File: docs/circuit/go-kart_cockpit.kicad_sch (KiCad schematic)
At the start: 40 parts, among them P1 Power, Q1 IRLIZ44N, SW1 SW_MEC_5E, X1 Taster rechts (male), X10 Display (male), X11 PD7, X12 SDA PG4, X13 AVR-ISP-10, X14 Taster links (male), X15 Start/Stop/Rückwärts, X2 5V GND, X3 24V Hupe, X4 SCL, X5 CS, X6 PB6, X7 J5, X8 J3, X9 Bluetooth-Modul

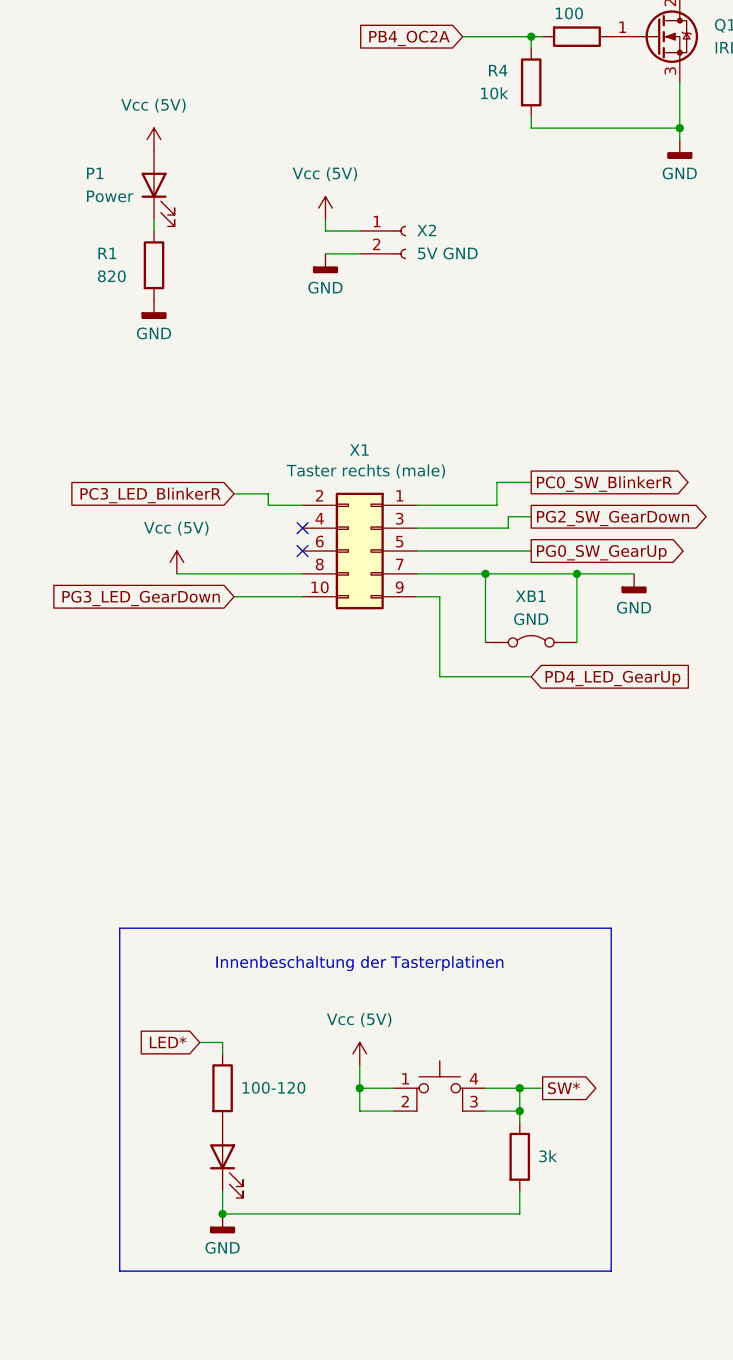
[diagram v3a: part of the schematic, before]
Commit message: feat: cleanup Tasterinnenbeschaltung for presentation
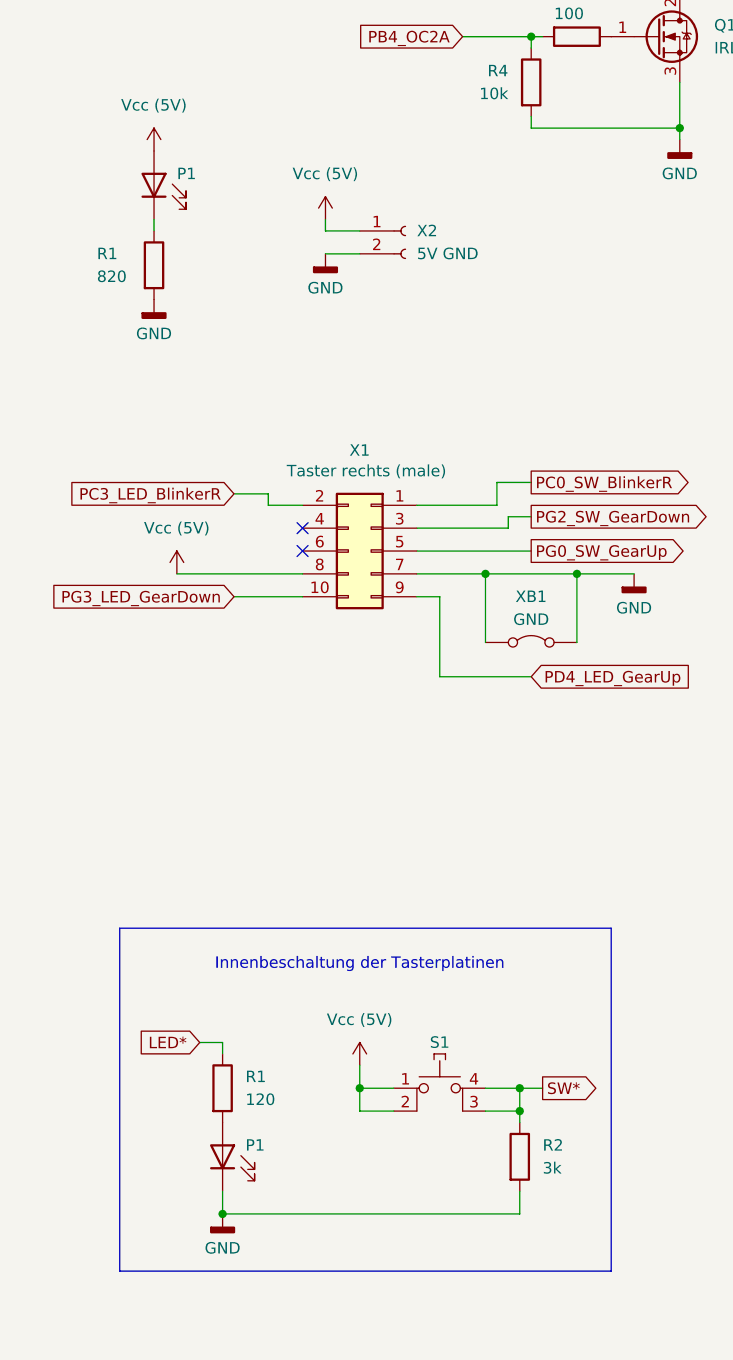
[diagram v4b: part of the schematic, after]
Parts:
- P1: renamed from D1; now left out of the parts list
- P1: value Power -> LED; footprint LED_THT:LED_D3.0mm_Horizontal_O1.27mm_Z6.0mm -> (none)
- R1: renamed from R2; value 100-120 -> 120; now left out of the parts list
- renumbered R3 to R2, SW1 to S1
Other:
- moved on the sheet: P1
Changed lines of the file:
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@@
 	)
 	(symbol
+		(lib_name "LED_1")
 		(lib_id "Device:LED")
 		(at 34.29 175.26 90)
 		(unit 1)
-		(exclude_from_sim no)
-		(in_bom yes)
+		(exclude_from_sim yes)
+		(in_bom no)
 		(on_board no)
 		(dnp no)
-		(fields_autoplaced yes)
-		(property "Reference" "D1"
-			(at 38.1 175.5774 90)
+		(property "Reference" "P1"
+			(at 36.83 173.99 90)
 			(effects
 				(font
@@
 				)
 				(justify right)
-				(hide yes)
 			)
 		)
@@
 			(project ""
 				(path "/e785e5e4-6da9-4e03-ba54-b62675208098"
-					(reference "D1")
+					(reference "P1")
 					(unit 1)
 				)
@@
 		(on_board no)
 		(dnp no)
-		(property "Reference" "R3"
-			(at 69.85 173.9899 0)
+		(property "Reference" "R2"
+			(at 69.85 173.99 0)
 			(effects
 				(font
@@
 				)
 				(justify left)
-				(hide yes)
 			)
 		)
 		(property "Value" "3k"
-			(at 69.342 175.26 0)
+			(at 69.85 176.53 0)
 			(effects
 				(font
@@
 			(project "go-kart_cockpit"
 				(path "/e785e5e4-6da9-4e03-ba54-b62675208098"
-					(reference "R3")
+					(reference "R2")
 					(unit 1)
 				)
@@
 		(dnp no)
 		(property "Reference" "P1"
-			(at 19.05 66.04 90)
+			(at 29.21 66.04 90)
 			(effects
 				(font
@@
 			)
 		)
-		(property "Value" "Power"
-			(at 19.05 68.58 90)
+		(property "Value" "LED"
+			(at 30.48 70.1674 90)
 			(effects
 				(font
@@
 				)
 				(justify right)
+				(hide yes)
 			)
 		)
-		(property "Footprint" "LED_THT:LED_D3.0mm_Horizontal_O1.27mm_Z6.0mm"
+		(property "Footprint" ""
 			(at 26.67 67.31 0)
 			(effects
@@
 		(on_board no)
 		(dnp no)
-		(fields_autoplaced yes)
-		(property "Reference" "SW1"
-			(at 58.42 160.02 0)
+		(property "Reference" "S1"
+			(at 58.42 162.56 0)
 			(effects
 				(font
 					(size 1.27 1.27)
 				)
-				(hide yes)
 			)
 		)
@@
 			(project ""
 				(path "/e785e5e4-6da9-4e03-ba54-b62675208098"
-					(reference "SW1")
+					(reference "S1")
 					(unit 1)
 				)
@@
 		(at 34.29 167.64 0)
 		(unit 1)
-		(exclude_from_sim no)
-		(in_bom yes)
+		(exclude_from_sim yes)
+		(in_bom no)
 		(on_board no)
 		(dnp no)
-		(property "Reference" "R2"
-			(at 36.83 166.3699 0)
+		(property "Reference" "R1"
+			(at 36.83 166.37 0)
 			(effects
 				(font
@@
 				)
 				(justify left)
-				(hide yes)
 			)
 		)
-		(property "Value" "100-120"
-			(at 36.322 167.64 0)
+		(property "Value" "120"
+			(at 36.83 168.91 0)
 			(effects
 				(font
@@
 			(project ""
 				(path "/e785e5e4-6da9-4e03-ba54-b62675208098"
-					(reference "R2")
+					(reference "R1")
 					(unit 1)
 				)

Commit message: feat: rework of PCB, fix wrong connection
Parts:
- removed P1: LED, symbol Device:LED
- removed X11: PD7, Connector_PinSocket_2.54mm:PinSocket_1x01_P2.54mm_Vertical, symbol Connector:Conn_01x01_Socket
- removed X12: SDA PG4, Connector_PinSocket_2.54mm:PinSocket_1x02_P2.54mm_Vertical, symbol Connector:Conn_01x02_Socket
- removed X2: 5V GND, Connector_PinSocket_2.54mm:PinSocket_1x02_P2.54mm_Vertical, symbol Connector:Conn_01x02_Socket
- removed XB10: ISP_SCK, Resistor_THT:R_Axial_DIN0207_L6.3mm_D2.5mm_P10.16mm_Horizontal, symbol Jumper:Jumper_2_Bridged
- removed XB4: Display_GND, Resistor_THT:R_Axial_DIN0207_L6.3mm_D2.5mm_P10.16mm_Horizontal, symbol Jumper:Jumper_2_Bridged
- removed XB5: Display_Vcc, Resistor_THT:R_Axial_DIN0207_L6.3mm_D2.5mm_P15.24mm_Horizontal, symbol Jumper:Jumper_2_Bridged
- removed XB9: ISP_MOSI, Resistor_THT:R_Axial_DIN0207_L6.3mm_D2.5mm_P15.24mm_Horizontal, symbol Jumper:Jumper_2_Bridged
- added P2: Power, LED_THT:LED_D3.0mm_Horizontal_O1.27mm_Z6.0mm, symbol Device:LED
- added X4: PC2 PG1 PD7, Connector_PinSocket_2.54mm:PinSocket_1x03_P2.54mm_Vertical, symbol Connector:Conn_01x03_Socket
- added X7: PD1 PG4 VCC GND, Connector_PinSocket_2.54mm:PinSocket_1x04_P2.54mm_Vertical, symbol Connector:Conn_01x04_Socket
- added XB1, XB6: GND, Resistor_THT:R_Axial_DIN0207_L6.3mm_D2.5mm_P10.16mm_Horizontal, symbol Jumper:Jumper_2_Bridged
- added XB11: MISO, TestPoint:TestPoint_2Pads_Pitch5.08mm_Drill1.3mm, symbol Jumper:Jumper_2_Bridged
- added XB12: /RESET, Resistor_THT:R_Axial_DIN0207_L6.3mm_D2.5mm_P15.24mm_Horizontal, symbol Jumper:Jumper_2_Bridged
- added XB2, XB3: Vcc, Resistor_THT:R_Axial_DIN0207_L6.3mm_D2.5mm_P10.16mm_Horizontal, symbol Jumper:Jumper_2_Bridged
- P1: value LED -> Power; footprint (none) -> LED_THT:LED_D3.0mm_Horizontal_O1.27mm_Z6.0mm
- Q1: value IRLIZ44N -> IRL3803; footprint Library:TO-220-3_Horizontal_TabDown_no_hole -> Package_TO_SOT_THT:TO-220F-3_Horizontal_TabDown
- R3: renamed from R1; footprint Resistor_THT:R_Axial_DIN0207_L6.3mm_D2.5mm_P10.16mm_Horizontal -> Resistor_THT:R_Axial_DIN0309_L9.0mm_D3.2mm_P12.70mm_Horizontal
- R4: renamed from R7; footprint Resistor_THT:R_Axial_DIN0207_L6.3mm_D2.5mm_P15.24mm_Horizontal -> Resistor_THT:R_Axial_DIN0207_L6.3mm_D2.5mm_P10.16mm_Horizontal
- R8: renamed from R1; value 120 -> 100-120; now in the parts list
- R9: renamed from R6; footprint Resistor_THT:R_Axial_DIN0309_L9.0mm_D3.2mm_P25.40mm_Horizontal -> Resistor_THT:R_Axial_DIN0207_L6.3mm_D2.5mm_P7.62mm_Horizontal
- XB4: renamed from XB3; value Display_Vcc -> Vcc
- renumbered R10 to R1, R2 to R10, R4 to R11, R11 to R2, R8 to R5, R9 to R6, R5 to R7, X15 to X1, X5 to X10, X8 to X11, X6 to X12, X3 to X14, X1 to X2, X14 to X3, X4 to X5, X7 to X6, X9 to X8, X10 to X9, XB6 to XB10, XB8 to XB5, XB1 to XB7, XB2 to XB8, XB7 to XB9
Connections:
- net +24V: now also X14.2 (Pin_2); no longer X14.3 (Pin_3)
- net GND: now also P2.1 (K), X7.4 (Pin_4), XB1.1 (A), XB1.2 (B), XB6.1 (A), XB6.2 (B)
- net Hupe (-): now also X14.3 (Pin_3); no longer X14.2 (Pin_2)
- net PB3_MISO: now also XB11.1 (A), XB11.2 (B)
- net PD1_SDA: now also X7.1 (Pin_1)
- net PD7: now also X4.3 (Pin_3)
- net PE0_RXD0: now also X9.2 (Pin_2); no longer X9.6 (Pin_6)
- net PE1_TXD0: now also X9.6 (Pin_6); no longer X9.2 (Pin_2)
- net PG4: now also X7.2 (Pin_2)
- net Vcc (5V): now also X7.3 (Pin_3), XB2.1 (A), XB2.2 (B), XB3.1 (A), XB3.2 (B)
- net /RESET: now also XB12.1 (A), XB12.2 (B)
- net at R8.2: now also P2.2 (A)
- net /PB7_SW_Reverse: now reaches X11.11 (Pin_11)
- net /PB7_SW_Reverse: now also R1.1
- net /PB5_SW_Start: now reaches X11.13 (Pin_13)
- net /PB5_SW_Start: now also R2.1
- net /PC2_SW_Start renamed PC2
- net PC2: now also X4.1 (Pin_1); no longer R2.1
- net /PG1_SW_Reverse renamed PG1
- net PG1: now also X4.2 (Pin_2); no longer R1.1
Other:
- moved on the sheet: P1, Q1, R1, R10, R11, R2, R3, R4, R5, R6, R7, R8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

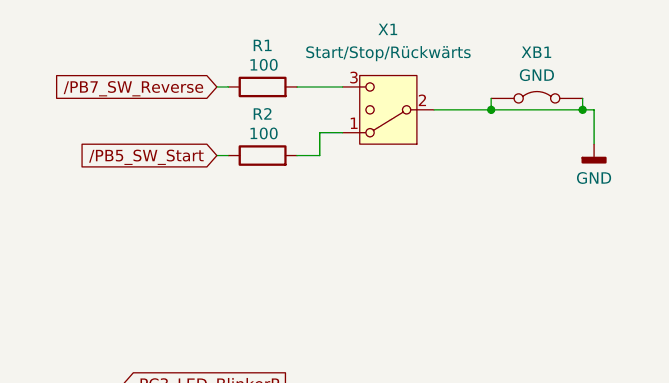
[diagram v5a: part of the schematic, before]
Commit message: feat(PCB): replace 100 ohm preresistors with 330
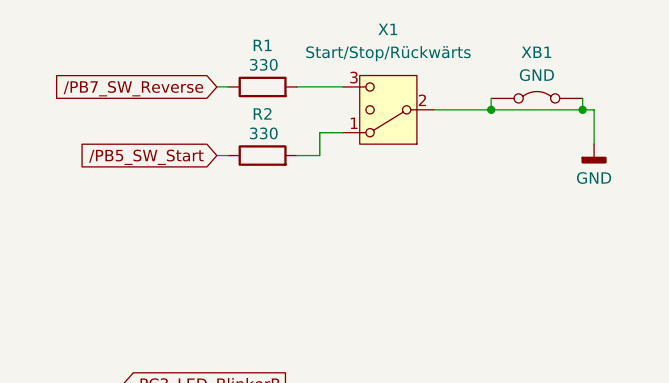
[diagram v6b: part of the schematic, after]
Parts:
- R1, R2: value 100 -> 330
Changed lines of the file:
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@@
 			)
 		)
-		(property "Value" "100"
+		(property "Value" "330"
 			(at 42.037 34.417 90)
 			(effects
@@
 			)
 		)
-		(property "Value" "100"
+		(property "Value" "330"
 			(at 42.037 26.797 90)
 			(effects

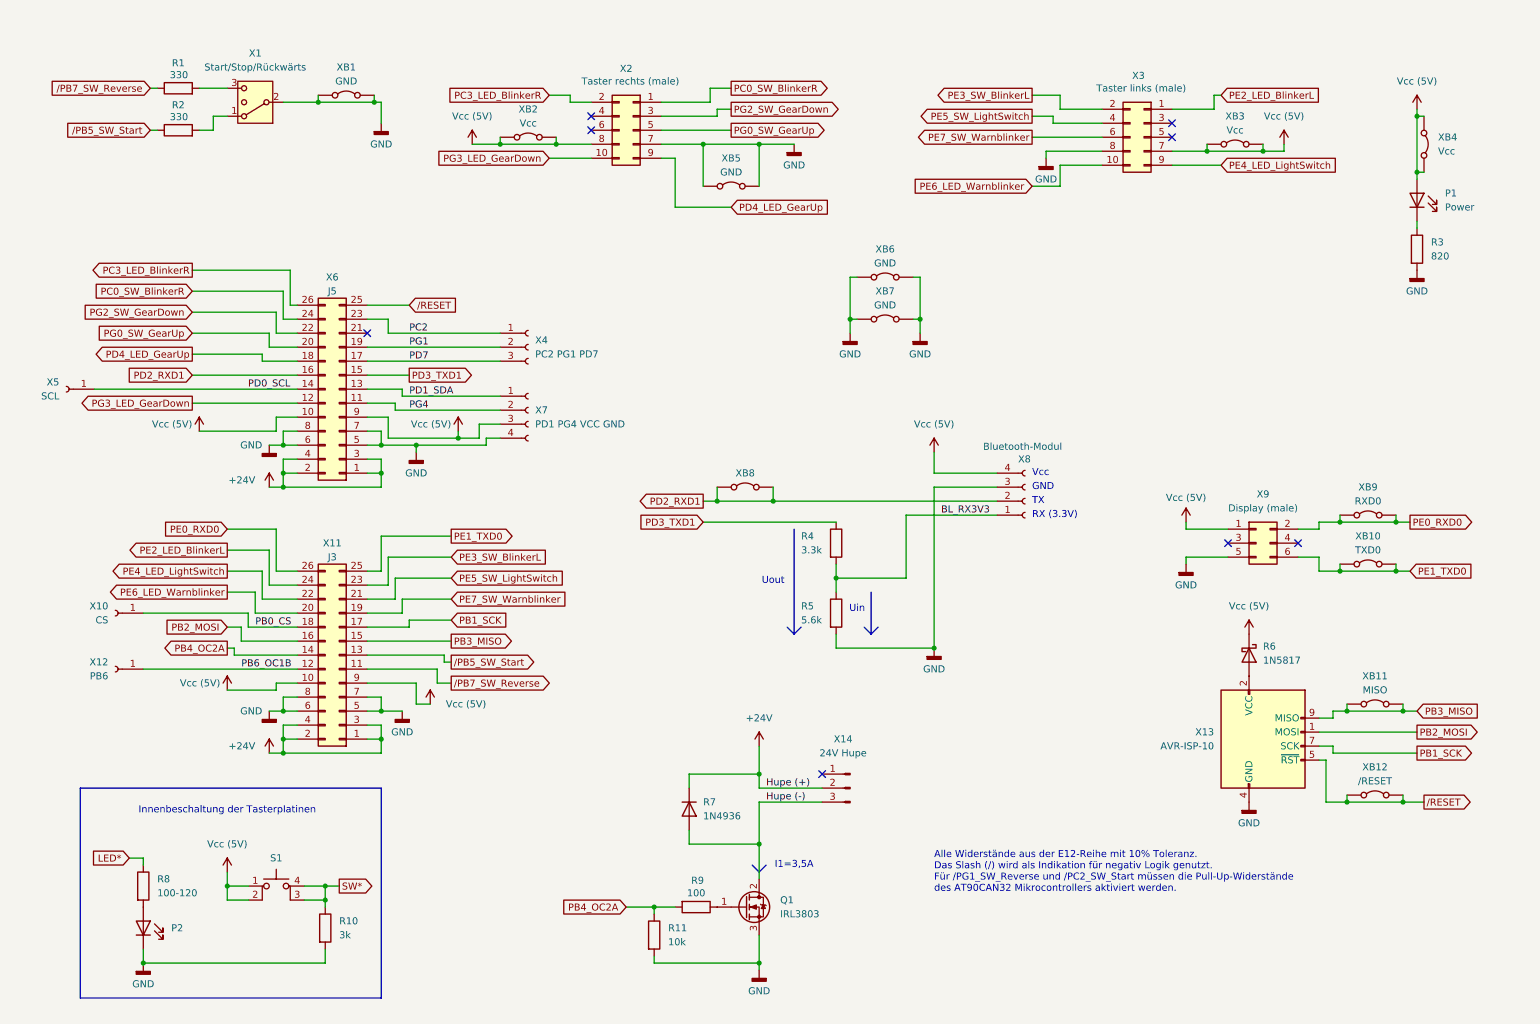
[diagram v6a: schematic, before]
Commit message: fix(PCB): ISP is actually connected to UART0 instead of SPI
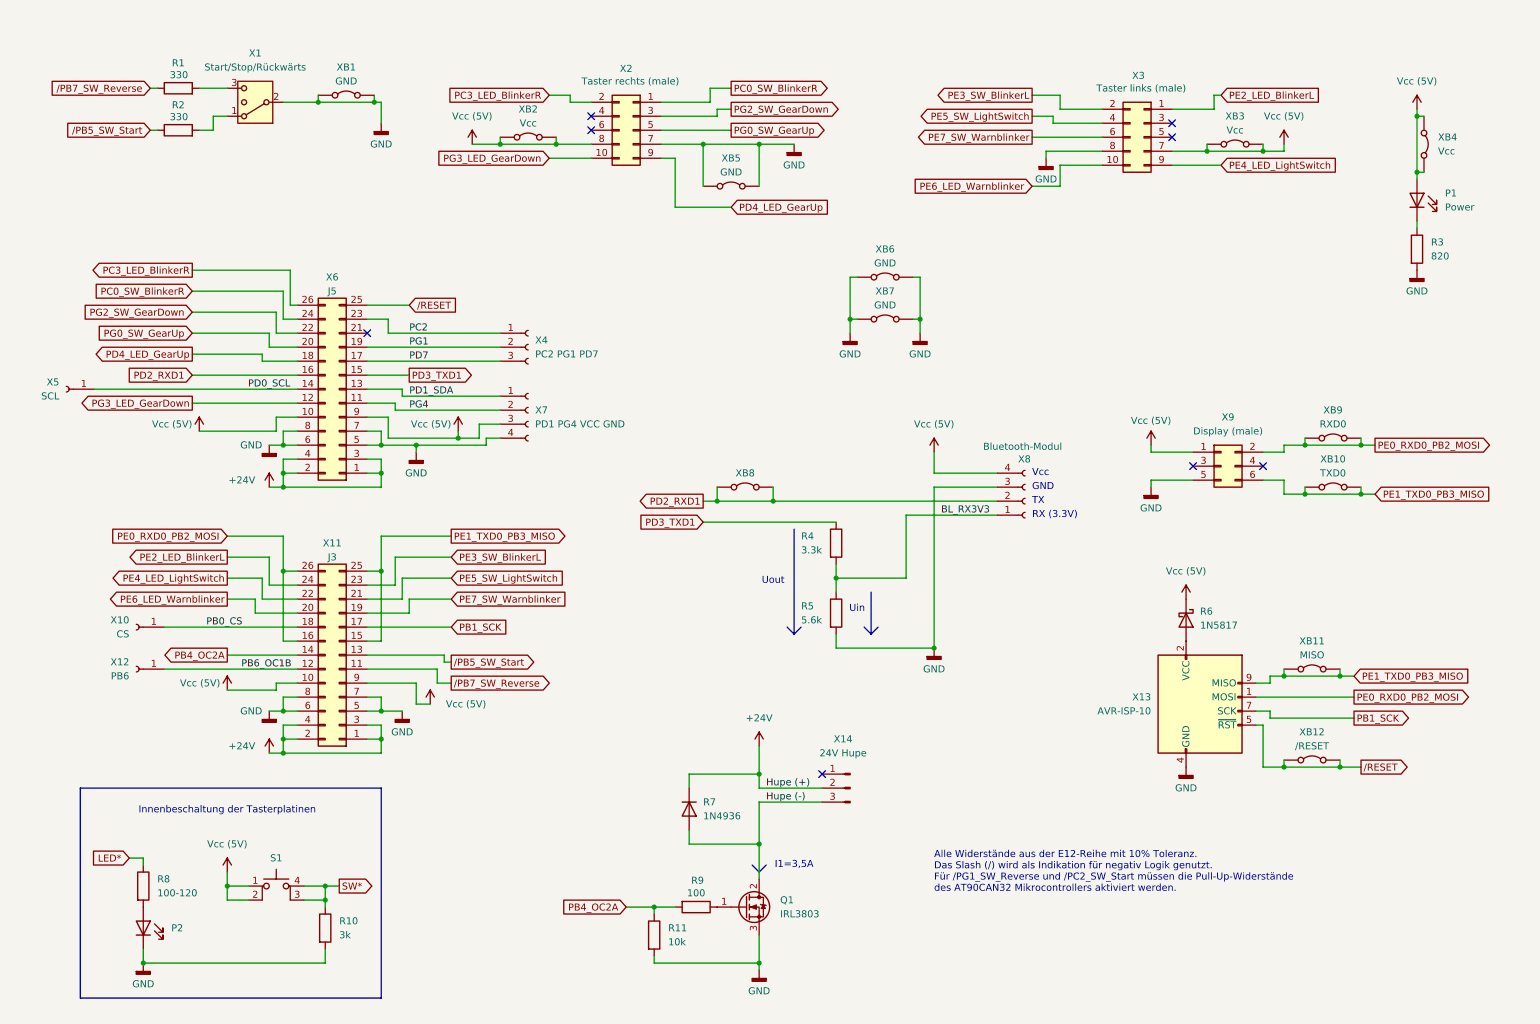
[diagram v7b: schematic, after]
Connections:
- net PE0_RXD0 is gone; now on net PE0_RXD0_PB2_MOSI: X11.26 (Pin_26), X9.2 (Pin_2), XB9.1 (A), XB9.2 (B)
- net PE1_TXD0 is gone; now on net PE1_TXD0_PB3_MISO: X11.25 (Pin_25), X9.6 (Pin_6), XB10.1 (A), XB10.2 (B)
- net PB2_MOSI renamed PE0_RXD0_PB2_MOSI
- net PB3_MISO renamed PE1_TXD0_PB3_MISO
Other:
- moved on the sheet: R6, X10, X12, X13, X9, XB10, XB11, XB12, XB9
